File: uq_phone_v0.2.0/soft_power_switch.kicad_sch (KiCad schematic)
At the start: 8 parts, among them Q4 DMP2035U-7, Q5 MMBT3904LP-7, SW42 SKSCLCE010

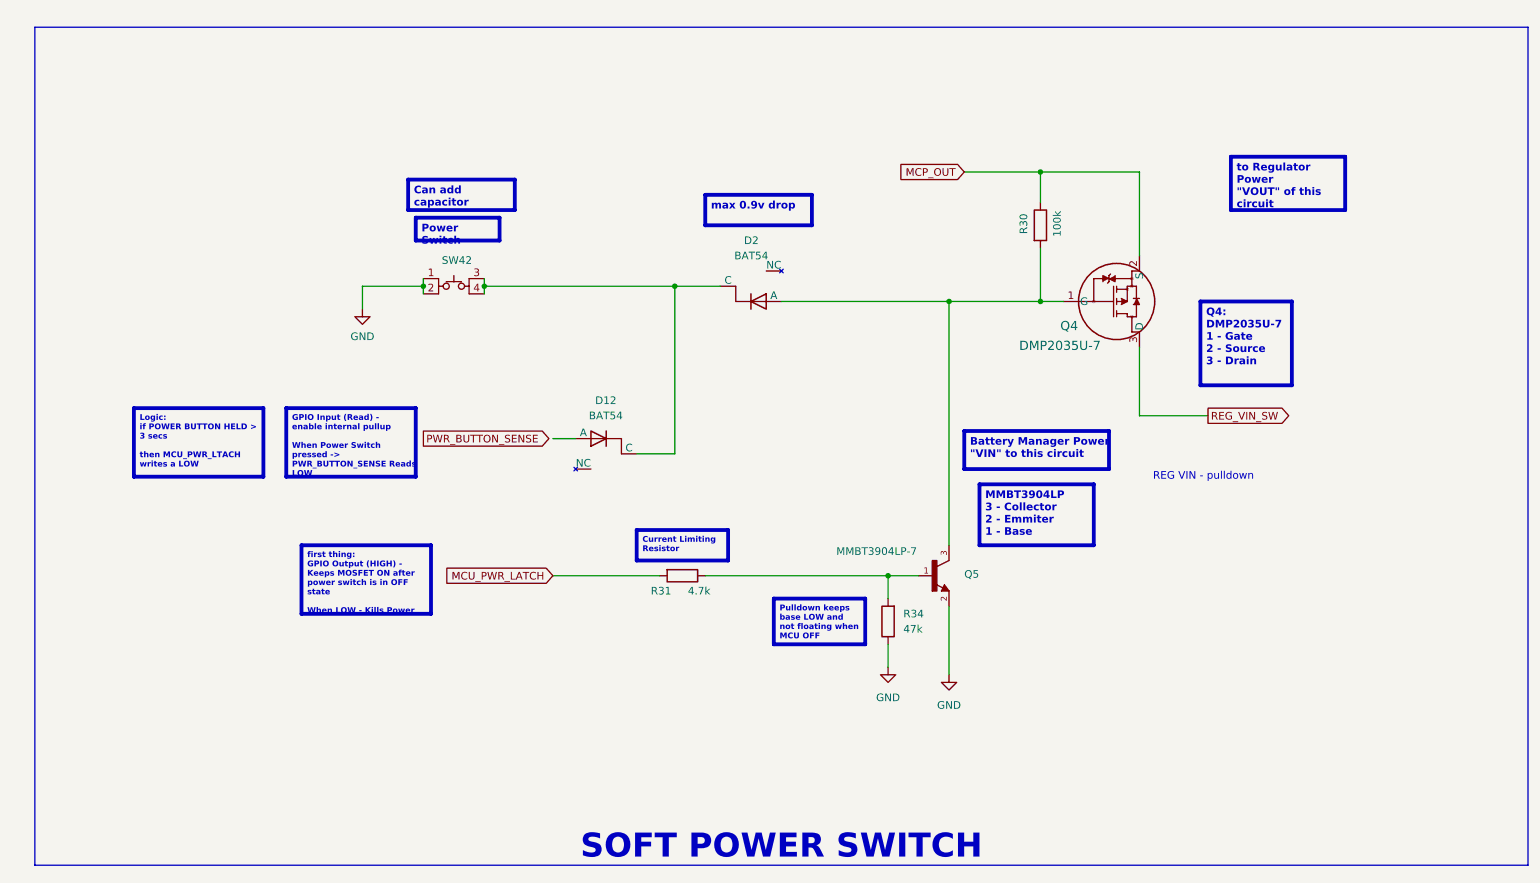
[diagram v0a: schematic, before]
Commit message: Fix KiCad libraries and update soft power circuit
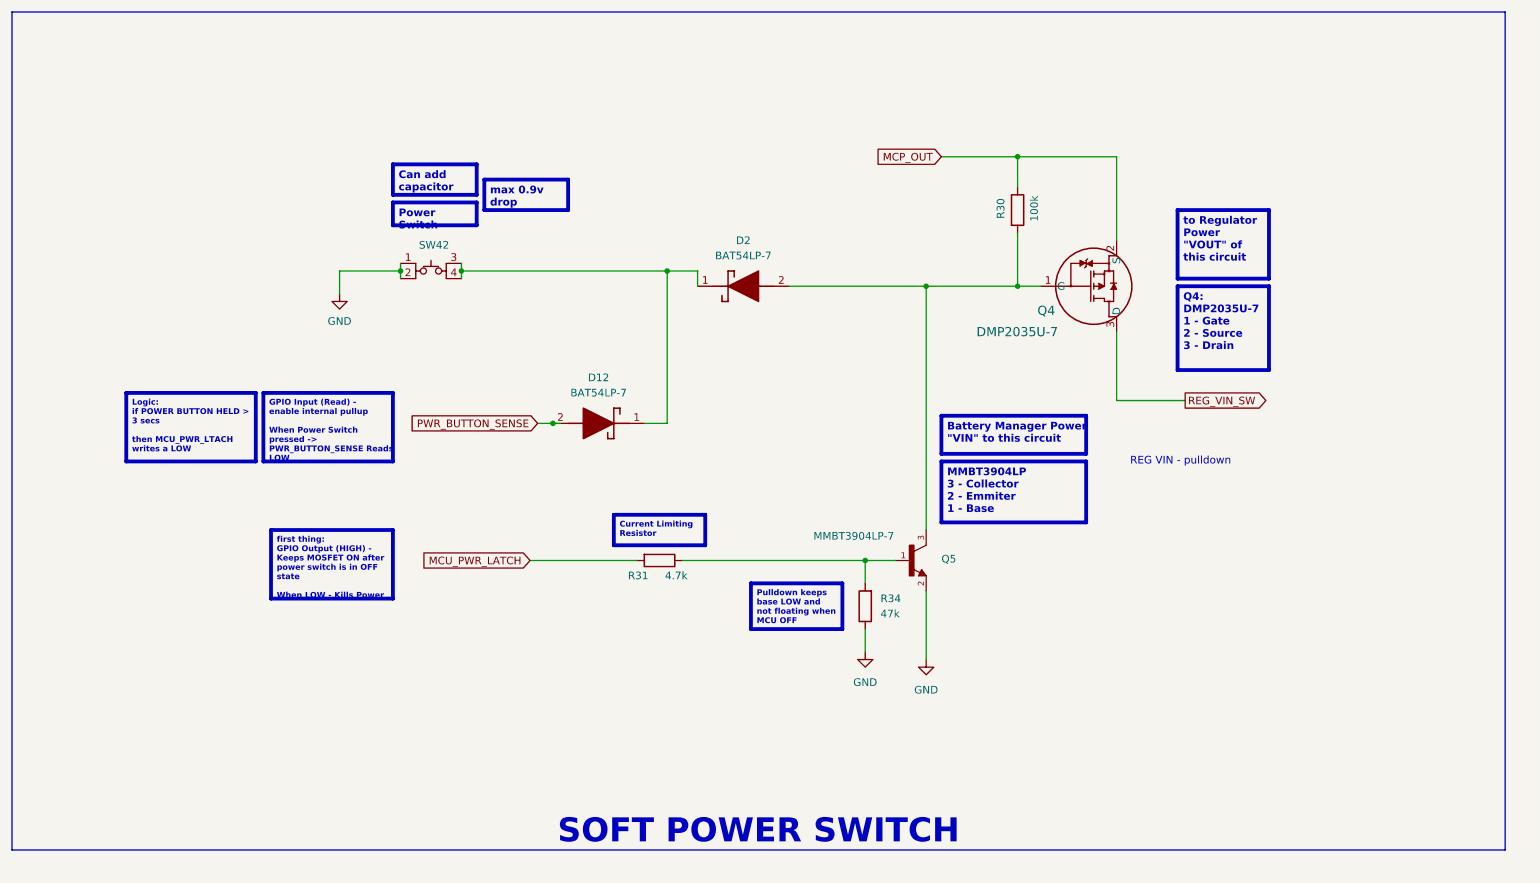
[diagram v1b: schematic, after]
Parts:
- removed D12, D2: BAT54, Package_TO_SOT_SMD:SOT-23-3, symbol BAT54:Diode-NC_pin
- added D12, D2: BAT54LP-7, BAT54LP-7:DESD3V3S1BL7B, symbol BAT54LP-7:BAT54LP-7
- Q5: footprint MMBT3904LP-7:DFN101X61X53-3N -> MMBT3904LP-7:MMBT3904LP7
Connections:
- net PWR_BUTTON_SENSE: now also D12.2 (A)
- net at Q4.1 (G), Q5.3, R30.2: now also D2.2 (A)
- net at SW42.3, SW42.4: now also D12.1 (K), D2.1 (K)
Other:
- moved on the sheet: Q4, Q5, R30, R31, R34, SW42

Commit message: Route soft power switch
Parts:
- removed SW42: SKSCLCE010, custom_footprints:SKSCLCE010, symbol Misc:SKSCLCE010
- added SW22: SKSCLCE010, custom_footprints:SKSCLCE010, symbol Misc:SKSCLCE010
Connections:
- net GND: now also SW22.1, SW22.2
- net at D12.1 (K), D2.1 (K): now also SW22.3, SW22.4
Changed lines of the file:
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@@
+	)
+	(symbol
+		(lib_id "Misc:SKSCLCE010")
+		(at 96.52 62.23 0)
+		(unit 1)
+		(exclude_from_sim no)
+		(in_bom yes)
+		(on_board yes)
+		(dnp no)
+		(property "Reference" "SW22"
+			(at 97.028 57.912 0)
+			(effects
+				(font
+					(size 1.27 1.27)
+				)
+			)
+		)
+		(property "Value" "SKSCLCE010"
+			(at 96.52 58.42 0)
+			(effects
+				(font
+					(size 1.27 1.27)
+				)
+				(hide yes)
+			)
+		)
+		(property "Footprint" "custom_footprints:SKSCLCE010"
+			(at 96.52 62.23 0)
+			(effects
+				(font
+					(size 1.27 1.27)
+				)
+				(hide yes)
+			)
+		)
+		(property "Datasheet" ""
+			(at 96.52 62.23 0)
+			(effects
+				(font
+					(size 1.27 1.27)
+				)
+				(hide yes)
+			)
+		)
+		(property "Description" ""
+			(at 96.52 62.23 0)
+			(effects
+				(font
+					(size 1.27 1.27)
+				)
+				(hide yes)
+			)
+		)
+		(property "LCSC PN" "C139799"
+			(at 96.52 62.23 0)
+			(effects
+				(font
+					(size 1.27 1.27)
+				)
+				(hide yes)
+			)
+		)
+		(property "DESCRIPTION" ""
+			(at 96.52 62.23 0)
+			(effects
+				(font
+					(size 1.27 1.27)
+				)
+				(hide yes)
+			)
+		)
+		(property "LSCS PN" ""
+			(at 96.52 62.23 0)
+			(effects
+				(font
+					(size 1.27 1.27)
+				)
+				(hide yes)
+			)
+		)
+		(pin "3"
+		)
+		(pin "4"
+		)
+		(pin "1"
+		)
+		(pin "2"
+		)
+		(instances
+			(project "uq_phone"
+				(path "/14f57415-6807-40a5-bb38-3cb818a2cdae/38b2de56-100e-42d4-87e1-7dc9ff9ca6c8"
+					(reference "SW22")
+					(unit 1)
+				)
+			)
+		)
 	)
 	(symbol
@@
 					(unit 1)
 				)
-			)
-		)
-	)
-	(symbol
-		(lib_id "Misc:SKSCLCE010")
-		(at 96.52 62.23 0)
-		(unit 1)
-		(exclude_from_sim no)
-		(in_bom yes)
-		(on_board yes)
-		(dnp no)
-		(property "Reference" "SW42"
-			(at 97.028 57.912 0)
-			(effects
-				(font
-					(size 1.27 1.27)
-				)
-			)
-		)
-		(property "Value" "SKSCLCE010"
-			(at 96.52 58.42 0)
-			(effects
-				(font
-					(size 1.27 1.27)
-				)
-				(hide yes)
-			)
-		)
-		(property "Footprint" "custom_footprints:SKSCLCE010"
-			(at 96.52 62.23 0)
-			(effects
-				(font
-					(size 1.27 1.27)
-				)
-				(hide yes)
-			)
-		)
-		(property "Datasheet" ""
-			(at 96.52 62.23 0)
-			(effects
-				(font
-					(size 1.27 1.27)
-				)
-				(hide yes)
-			)
-		)
-		(property "Description" ""
-			(at 96.52 62.23 0)
-			(effects
-				(font
-					(size 1.27 1.27)
-				)
-				(hide yes)
-			)
-		)
-		(property "LCSC PN" "C139799"
-			(at 96.52 62.23 0)
-			(effects
-				(font
-					(size 1.27 1.27)
-				)
-				(hide yes)
-			)
-		)
-		(property "DESCRIPTION" ""
-			(at 96.52 62.23 0)
-			(effects
-				(font
-					(size 1.27 1.27)
-				)
-				(hide yes)
-			)
-		)
-		(property "LSCS PN" ""
-			(at 96.52 62.23 0)
-			(effects
-				(font
-					(size 1.27 1.27)
-				)
-				(hide yes)
-			)
-		)
-		(pin "3"
-		)
-		(pin "4"
-		)
-		(pin "1"
-		)
-		(pin "2"
-		)
-		(instances
-			(project "uq_phone"
-				(path "/14f57415-6807-40a5-bb38-3cb818a2cdae/38b2de56-100e-42d4-87e1-7dc9ff9ca6c8"
-					(reference "SW42")
-					(unit 1)
-				)
-			)
-			(project "soft_power_switch"
-				(path "/b158ef66-b62f-40c2-905d-91f68d4b257c"
-					(reference "SW1")
-					(unit 1)
-				)

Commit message: Save PCB and schematic before STM32 FMC pin remapping
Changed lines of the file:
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@@
 	(text_box "SOFT POWER SWITCH\n"
 		(exclude_from_sim no)
-		(at 26.67 19.05 0)
-		(size 248.92 139.7)
+		(at 26.67 25.4 0)
+		(size 248.92 128.27)
 		(margins 0.9525 0.9525 0.9525 0.9525)
 		(stroke

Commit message: Add GPIO expander and 16-bit FMC display schematic
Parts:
- renumbered D2 to D14
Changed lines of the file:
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@@
-				)
-			)
-			(project "soft_power_switch"
-				(path "/b158ef66-b62f-40c2-905d-91f68d4b257c"
-					(reference "#PWR0102")
-					(unit 1)
 				)
 			)
@@
 				)
 			)
-			(project "soft_power_switch"
-				(path "/b158ef66-b62f-40c2-905d-91f68d4b257c"
-					(reference "#PWR0101")
-					(unit 1)
-				)
-			)
 		)
 	)
@@
 				)
 			)
-			(project "soft_power_switch"
-				(path "/b158ef66-b62f-40c2-905d-91f68d4b257c"
-					(reference "#PWR0103")
-					(unit 1)
-				)
-			)
 		)
 	)
@@
 				)
 			)
-			(project "soft_power_switch"
-				(path "/b158ef66-b62f-40c2-905d-91f68d4b257c"
-					(reference "Q1")
-					(unit 1)
-				)
-			)
 		)
 	)
@@
 		(dnp no)
 		(fields_autoplaced yes)
-		(property "Reference" "D2"
+		(property "Reference" "D14"
 			(at 148.59 57.15 0)
 			(effects
@@
 			(project ""
 				(path "/14f57415-6807-40a5-bb38-3cb818a2cdae/38b2de56-100e-42d4-87e1-7dc9ff9ca6c8"
-					(reference "D2")
+					(reference "D14")
 					(unit 1)
 				)
@@
 				)
 			)
-			(project "soft_power_switch"
-				(path "/b158ef66-b62f-40c2-905d-91f68d4b257c"
-					(reference "Q2")
-					(unit 1)
-				)
-			)
 		)
 	)
@@
 				)
 			)
-			(project "soft_power_switch"
-				(path "/b158ef66-b62f-40c2-905d-91f68d4b257c"
-					(reference "R2")
-					(unit 1)
-				)
-			)
 		)
 	)
@@
 				)
 			)
-			(project "soft_power_switch"
-				(path "/b158ef66-b62f-40c2-905d-91f68d4b257c"
-					(reference "R3")
-					(unit 1)
-				)
-			)
 		)
 	)
@@
 					(unit 1)
 				)
-			)
-			(project "soft_power_switch"
-				(path "/b158ef66-b62f-40c2-905d-91f68d4b257c"
-					(reference "R1")
-					(unit 1)
-				)
